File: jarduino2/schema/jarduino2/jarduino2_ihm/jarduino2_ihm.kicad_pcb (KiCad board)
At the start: 2 copper layers, 119 x 29 mm, 18 parts, among them J1 Alim CPU, J2 Alim CPU, J3 Indicateurs, J4 Pompes, SW1 Pile On/Off, SW2 POW ON/OFF, SW3 Pile On/Off, SW4 Pompe 1, SW5 Pompe 2

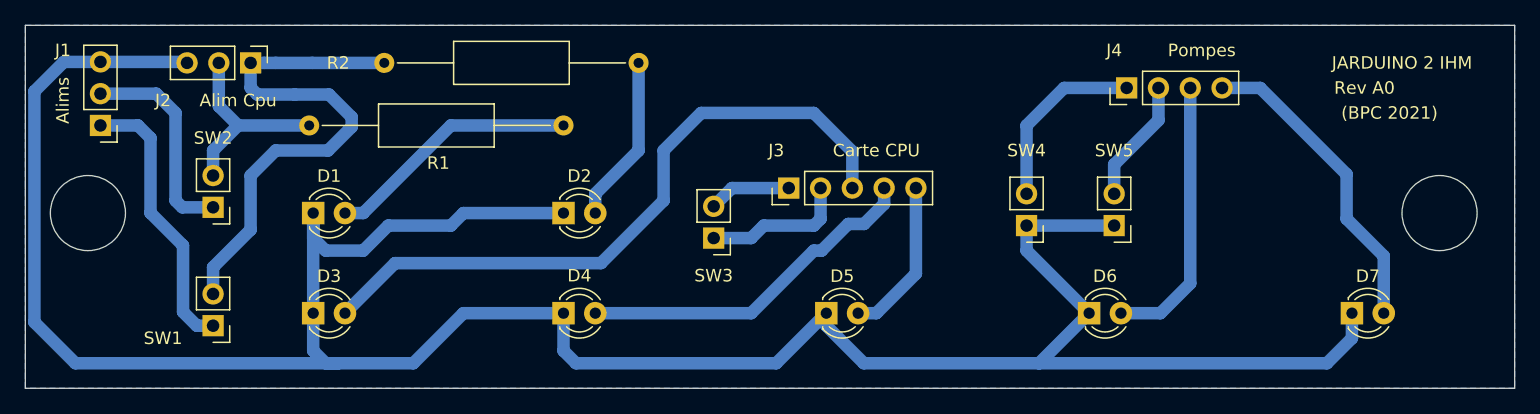
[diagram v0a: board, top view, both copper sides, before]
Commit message: Amélioration proto: - Diametre trous de fixation 4mm (avec compo sepcial) - SW1/SW2 echanges Batt/Sol
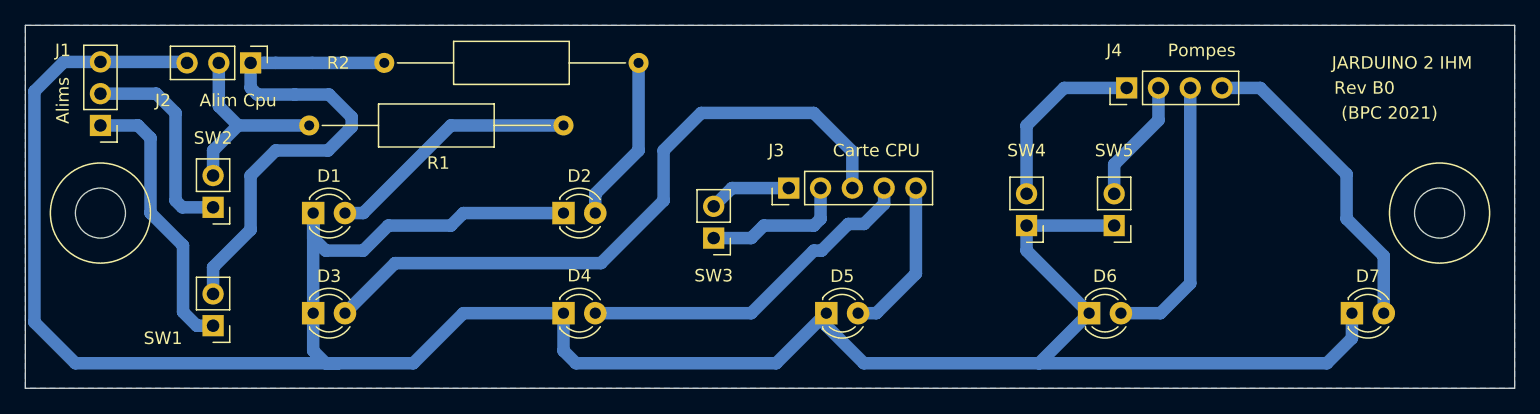
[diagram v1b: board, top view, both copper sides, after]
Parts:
- added REF**: BPC_Trou4mm_Fixation, bpc:BPC_Trou4mm_Fixation, F.Cu at (208.0, 110.0)
- added REF**: BPC_Trou4mm_Fixation, bpc:BPC_Trou4mm_Fixation, F.Cu at (101.0, 110.0)
- D1: value Batt Pow OK -> Solaire OK
- D2: value Solaire OK -> Batterie OK
- SW1: value Pile On/Off -> Batterie On/Off
- SW2: value POW ON/OFF -> Solaire ON/OFF
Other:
- outline, holes or cut-outs redrawn
- board text added: "Rev B0"
- board text removed: "Rev A0"
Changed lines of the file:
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@@
   (general
     (thickness 1.6)
-    (drawings 14)
+    (drawings 12)
     (tracks 113)
     (zones 0)
-    (modules 18)
+    (modules 20)
     (nets 17)
   )
   (page A4)
   (layers
-    (0 F.Cu signal hide)
-    (31 B.Cu signal)
+    (0 F.Cu signal)
+    (31 B.Cu signal hide)
     (32 B.Adhes user hide)
     (33 F.Adhes user hide)
@@
     (35 F.Paste user hide)
     (36 B.SilkS user hide)
-    (37 F.SilkS user hide)
+    (37 F.SilkS user)
     (38 B.Mask user)
     (39 F.Mask user hide)
@@
   )
   (setup
-    (last_trace_width 1)
+    (last_trace_width 0.25)
     (user_trace_width 1)
     (trace_clearance 0.2)
@@
     (aux_axis_origin 0 0)
     (grid_origin 95 95)
-    (visible_elements FFFFFF7F)
+    (visible_elements 7FFFFFFF)
     (pcbplotparams
       (layerselection 0x01060_fffffffe)
@@
     (add_net "Net-(J4-Pad2)")
   )
+  (module bpc:BPC_Trou4mm_Fixation (layer F.Cu)
+    (at 208 110)
+    (fp_text reference REF** (at -6 -3) (layer F.Fab) hide
+      (effects (font (size 1 1) (thickness 0.15)))
+    )
+    (fp_text value BPC_Trou4mm_Fixation (at 0 -6) (layer F.Fab)
+      (effects (font (size 1 1) (thickness 0.15)))
+    )
+    (fp_circle (center 0 0) (end 4 0) (layer F.SilkS) (width 0.12))
+    (pad "" np_thru_hole circle (at 0 0) (size 4 4) (drill 4) (layers *.Cu *.Mask))
+  )
+  (module bpc:BPC_Trou4mm_Fixation (layer F.Cu)
+    (at 101 110)
+    (fp_text reference REF** (at 4 -4) (layer F.Fab) hide
+      (effects (font (size 1 1) (thickness 0.15)))
+    )
+    (fp_text value BPC_Trou4mm_Fixation (at 0 -6) (layer F.Fab)
+      (effects (font (size 1 1) (thickness 0.15)))
+    )
+    (fp_circle (center 0 0) (end 4 0) (layer F.SilkS) (width 0.12))
+    (pad "" np_thru_hole circle (at 0 0) (size 4 4) (drill 4) (layers *.Cu *.Mask))
+  )
   (module Connector_PinHeader_2.54mm:PinHeader_1x04_P2.54mm_Vertical (layer F.Cu)
     (at 183 100 90)
@@
       (effects (font (size 1 1) (thickness 0.15)))
     )
-    (fp_text value "POW ON/OFF" (at 0 5.54) (layer F.Fab)
+    (fp_text value "Solaire ON/OFF" (at 0 5.54) (layer F.Fab)
       (effects (font (size 1 1) (thickness 0.15)))
     )
@@
       (effects (font (size 1 1) (thickness 0.15)))
     )
-    (fp_text value "Pile On/Off" (at 0 5) (layer F.Fab)
+    (fp_text value "Batterie On/Off" (at 0 5) (layer F.Fab)
       (effects (font (size 1 1) (thickness 0.15)))
     )
@@
       (effects (font (size 1 1) (thickness 0.15)))
     )
-    (fp_text value "Solaire OK" (at 1.27 2.96) (layer F.Fab)
+    (fp_text value "Batterie OK" (at 1.27 2.96) (layer F.Fab)
       (effects (font (size 1 1) (thickness 0.15)))
     )
@@
       (effects (font (size 1 1) (thickness 0.15)))
     )
-    (fp_text value "Batt Pow OK" (at 1.27 2.96) (layer F.Fab)
+    (fp_text value "Solaire OK" (at 1.27 2.96) (layer F.Fab)
       (effects (font (size 1 1) (thickness 0.15)))
     )
@@
     (effects (font (size 1 1) (thickness 0.15)))
   )
-  (gr_text "Rev A0" (at 202 100) (layer F.SilkS)
+  (gr_text "Rev B0" (at 202 100) (layer F.SilkS)
     (effects (font (size 1 1) (thickness 0.15)))
   )
@@
   (gr_line (start 214 124) (end 95 124) (layer Edge.Cuts) (width 0.05))
   (gr_line (start 214 95) (end 214 124) (layer Edge.Cuts) (width 0.05))
-  (gr_circle (center 208 110) (end 211 110) (layer Edge.Cuts) (width 0.05))
   (gr_line (start 95 95) (end 95 108) (layer Edge.Cuts) (width 0.05))
-  (gr_circle (center 100 110) (end 103 110) (layer Edge.Cuts) (width 0.05))
   (gr_line (start 95 95) (end 214 95) (layer Edge.Cuts) (width 0.05))
   (segment (start 120.54 110) (end 122 110) (width 1) (layer B.Cu) (net 1))
